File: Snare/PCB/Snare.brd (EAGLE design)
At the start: 100 x 50 mm, 2 parts

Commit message: Finished Schematic
Finished Schematic
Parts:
- added 100K, 47K, R39, R40, R43: 2k, resistor:0207/10
- added C15, C48: 0.33uF, resistor:C050-024X044
- added C2, C21, C22, C3, C30, C34, C35, C36, C37, C39, C40, C43, C44, C45, C49, C50: 0.1uF, resistor:C050-024X044
- added C20, C38: 1nF, resistor:C050-024X044
- added C23, C41: 2.2u, resistor:C050-024X044
- added C24, C28, C31, C32, C33, C42: 10uF, rcl:E2,5-6
- added C26, C27, C29: 1u, resistor:C050-024X044
- added C46, C47: 33nF, resistor:C050-024X044
- added D6: 200mA/100V/1V, SparkFun-DiscreteSemi:DIODE-1N4148
- added IC1, IC10, IC6, IC7, IC8, IC9: LM741P, linear:DIL08
- added Q3, Q4: 2N2222A, SparkFun-DiscreteSemi:TO-92
- added R1, R3, R4, R45, R47, R48, R49, R5, R58, R59, R60, R61, R7, R9: 10k, resistor:0207/10
- added R10, R57, R62, R8: 10k, rcl:RTRIM64W
- added R2, R36, R53: 100k, resistor:0207/10
- added R34: 680k, resistor:0207/10
- added R35, R54, R56, R6: 1k, resistor:0207/10
- added R38: 4.7k, resistor:0207/10
- added R44, R46: 15k, resistor:0207/10
- added R50: 220, resistor:0207/10
- added R51, R67: 47k, resistor:0207/10
- added R52, R65: 470k, resistor:0207/10
- added R55: 1meg, resistor:0207/10
- added R63: 20 OHM, rcl:RTRIM64W
- added R64: 100, resistor:0207/10
- added R66: 51k, resistor:0207/10
- added T1, T5, T6: 2N3904, transistor:TO92
- added U$1: (no value), Capstone:TO-92
- D1: value 1N4148 -> 200mA/100V/1V
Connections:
- net 0V renamed POT5B
- net POT5 renamed POT3A
- net POT6_7 renamed POT3B
- net POT7 renamed POT4A
- net POT8 renamed POT4B
- net POT9 renamed POT5A
- removed net POT1: SV1.6
- removed net POT2: SV1.5
- removed net POT3: SV1.8
- removed net POT4: SV1.7
- new net CC_INPUT: C23.2, IC1.6, R8.2
- new net LOW_FREQ_WN: IC8.6, R3.2, R45.1
- new net N$1: R3.1, R4.2, R5.1
- new net N$17: T1.2, T5.2
- new net N$2: IC1.2, R6.2, R7.1, R9.1
- new net N$20: C30.1, R34.2, T1.3
- new net N$21: C31.-, C33.-, C34.1, R35.2, R36.2, R40.1
- new net N$23: 100K.2, 47K.1, IC6.2
- new net N$27: IC7.2, R43.2
- new net N$28: 47K.2, C35.1
- new net N$3: R6.1, R8.1
- new net N$30: C32.+, R38.2, T5.1
- new net N$32: C38.1, IC7.3, R44.1
- new net N$33: IC8.2, R1.1, R45.2
- new net N$34: C20.1, IC8.3, R46.2
- new net N$36: C15.2, C43.2, D1.C, R53.2
- new net N$37: C23.1, R47.1, R48.2, T6.2
- new net N$38: C41.1, R49.2, T6.3
- new net N$39: C26.1, C42.+, R50.1, T6.1
- new net N$4: IC1.5, R10.1
- new net N$40: D1.A, Q3.3, R52.2
- new net N$41: C43.1, IC9.3, R54.2
- new net N$42: R63.2, R64.2
- new net N$43: C46.2, IC9.2, R55.2
- new net N$44: C46.1, C47.2
- new net N$45: IC9.1, R57.3
- new net N$46: IC9.5, R57.1
- new net N$48: IC10.3, R59.2, R61.1, R63.1
- new net N$49: IC10.2, R58.1, R60.2, U$1.1
- new net N$5: C31.+, R35.1, T5.3
- new net N$50: IC10.1, R62.3
- new net N$51: C48.2, D6.C, R66.2
- new net N$52: IC10.5, R62.1
- new net N$53: D6.A, Q4.3, R65.2
- new net N$6: C30.2, C33.+, C34.2, R34.1, R38.1, R39.2
- new net N$7: IC1.1, R10.3
- new net POT1A: C47.1, IC9.6, R55.1, R56.2, SV1.6
- new net POT1B: R7.2, SV1.5
- new net POT2A: IC7.6, R43.1, SV1.8
- new net POT2B: R5.2, SV1.7
- new net VCA_INPUT: R4.1, R58.2, R61.2
- new net VCA_OUT: IC10.6, R60.1, R9.2
- new net VCA_TRIGGER: R66.1, R67.2, U$1.2
- new net WHITE_NOISE: C32.-, C35.2, R36.1
- new net WHITE_NOISE_AMP: 100K.1, C38.2, IC6.6, R2.1, R46.1
- net +12V: now also C22.2, C24.+, C27.2, C3.2, C37.2, C40.2, C45.1, C50.2, IC1.7, IC10.7, IC6.7, IC7.7, IC8.7, IC9.7, Q3.1, Q4.1, R39.1, R47.2, R50.2
- net -12V: now also C2.2, C21.2, C28.-, C29.1, C36.2, C39.2, C44.2, C49.2, IC1.4, IC10.4, IC6.4, IC7.4, IC8.4, IC9.4, R10.2, R40.2, R48.1, R49.1, R57.2, R62.2
- net AGND: now also C15.1, C2.1, C20.2, C21.1, C22.1, C24.-, C26.2, C27.1, C28.+, C29.2, C3.1, C36.1, C37.1, C39.1, C40.1, C42.-, C44.1, C45.2, C48.1, C49.1, C50.1, IC1.3, IC6.3, R1.2, R2.2, R44.2, R51.1, R52.1, R53.1, R54.1, R56.1, R59.1, R64.1, R65.1, R67.1, U$1.3
- net OUTPUT: now also C41.2, R51.2
- net TRIGGER: now also Q3.2, Q4.2
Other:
- board text removed: "Drum - Generic Feb 2019 Koltin Kosik-Harvey"

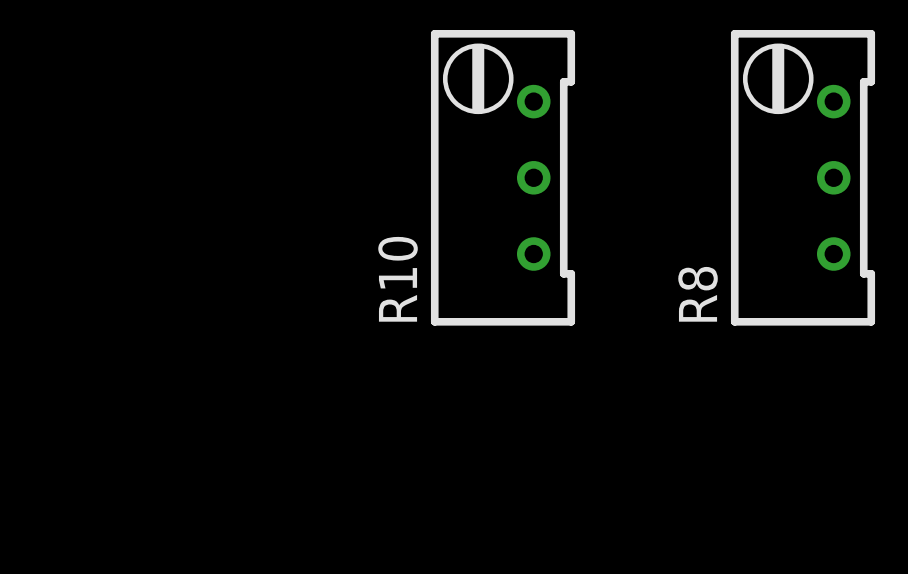
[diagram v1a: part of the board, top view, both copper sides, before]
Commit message: Updated Snare schematic
updated snare schematic
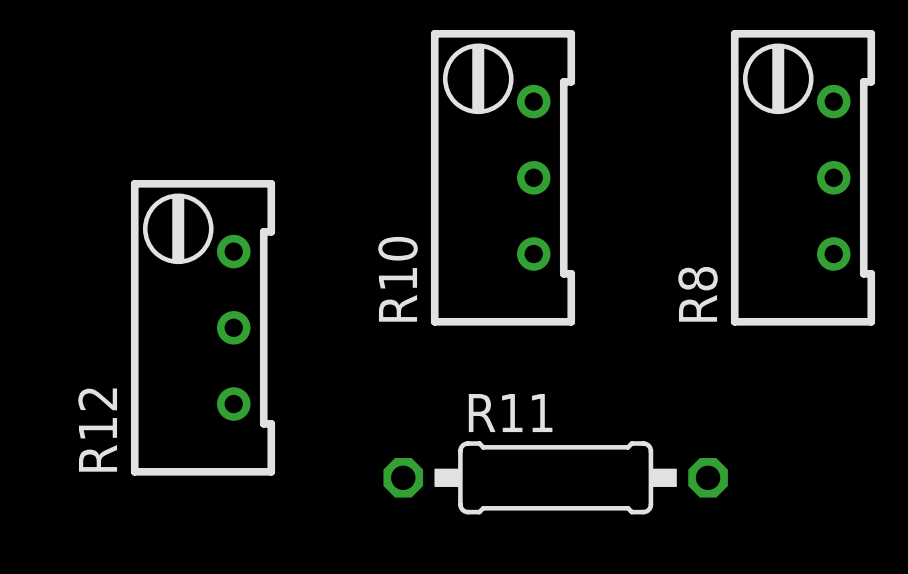
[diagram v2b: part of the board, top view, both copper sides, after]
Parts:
- added R11: 4.7k, resistor:0207/10
- added R12: 10k, rcl:RTRIM64W
- R1: value 10k -> 2k
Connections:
- removed net VCA_OUT: IC10.6, R60.1, R9.2
- new net DRUM_OUTPUT: C47.1, IC9.6, R12.3, R55.1, R56.2
- net AGND: now also R11.2, R12.1
- net N$27: now also R11.1
- net POT1A: now also R12.2; no longer C47.1, IC9.6, R55.1, R56.2
- net SW1: now also IC10.6, R60.1
- net SW2: now also R9.2
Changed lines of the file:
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@@
 <attribute name="VALUE" x="120.7394" y="-148.635" size="1.27" layer="27" ratio="10"/>
 </element>
-<element name="R1" library="resistor" library_urn="urn:adsk.eagle:library:348" package="0207/10" package3d_urn="urn:adsk.eagle:package:25939/1" value="10k" x="4" y="-160" smashed="yes">
+<element name="R1" library="resistor" library_urn="urn:adsk.eagle:library:348" package="0207/10" package3d_urn="urn:adsk.eagle:package:25939/1" value="2k" x="4" y="-160" smashed="yes">
 <attribute name="NAME" x="0.952" y="-158.476" size="1.27" layer="25" ratio="10"/>
 <attribute name="VALUE" x="1.7394" y="-160.635" size="1.27" layer="27" ratio="10"/>
@@
 <attribute name="SPICEPREFIXL" value="POT" x="-17" y="-216" size="1.778" layer="27" display="off"/>
 <attribute name="VALUE" x="-12.65" y="-220.95" size="1.27" layer="27" rot="R90"/>
+</element>
+<element name="R11" library="resistor" library_urn="urn:adsk.eagle:library:348" package="0207/10" package3d_urn="urn:adsk.eagle:package:25939/1" value="4.7k" x="-15" y="-226" smashed="yes">
+<attribute name="NAME" x="-18.048" y="-224.476" size="1.27" layer="25" ratio="10"/>
+<attribute name="VALUE" x="-17.2606" y="-226.635" size="1.27" layer="27" ratio="10"/>
+</element>
+<element name="R12" library="rcl" library_urn="urn:adsk.eagle:library:334" package="RTRIM64W" package3d_urn="urn:adsk.eagle:package:23748/1" value="10k" x="-27" y="-221" smashed="yes">
+<attribute name="NAME" x="-29.62" y="-225.95" size="1.27" layer="25" rot="R90"/>
+<attribute name="SPICEMODEL" value="X" x="-27" y="-221" size="1.778" layer="27" display="off"/>
+<attribute name="SPICEPREFIXL" value="POT" x="-27" y="-221" size="1.778" layer="27" display="off"/>
+<attribute name="VALUE" x="-22.65" y="-225.95" size="1.27" layer="27" rot="R90"/>
 </element>
 </elements>
@@
 <signal name="SW2">
 <contactref element="SV1" pad="20"/>
+<contactref element="R9" pad="2"/>
+<wire x1="40.64" y1="12.7" x2="9.08" y2="-221" width="0" layer="19" extent="1-1"/>
 </signal>
 <signal name="SW1">
 <contactref element="SV1" pad="18"/>
+<contactref element="IC10" pad="6"/>
+<contactref element="R60" pad="1"/>
+<wire x1="43.18" y1="12.7" x2="68.27" y2="42.81" width="0" layer="19" extent="1-1"/>
+<wire x1="4" y1="37.92" x2="43.18" y2="12.7" width="0" layer="19" extent="1-1"/>
 </signal>
 <signal name="TRIGGER">
@@
 <contactref element="IC1" pad="3"/>
 <contactref element="C20" pad="2"/>
-<wire x1="165.46" y1="71" x2="172.46" y2="78" width="0" layer="19" extent="1-1"/>
-<wire x1="175.08" y1="64" x2="165.46" y2="71" width="0" layer="19" extent="1-1"/>
-<wire x1="172.46" y1="50" x2="175.08" y2="64" width="0" layer="19" extent="1-1"/>
-<wire x1="170.54" y1="50" x2="172.46" y2="50" width="0" layer="19" extent="1-1"/>
+<contactref element="R11" pad="2"/>
+<contactref element="R12" pad="1"/>
+<wire x1="-9.92" y1="-226" x2="-25.73" y2="-223.54" width="0" layer="19" extent="1-1"/>
+<wire x1="-0.54" y1="-194" x2="-9.92" y2="-226" width="0" layer="19" extent="1-1"/>
+<wire x1="6.46" y1="-194" x2="-0.54" y2="-194" width="0" layer="19" extent="1-1"/>
+<wire x1="9.08" y1="-165" x2="6.46" y2="-194" width="0" layer="19" extent="1-1"/>
+<wire x1="9.08" y1="-160" x2="9.08" y2="-165" width="0" layer="19" extent="1-1"/>
+<wire x1="117.92" y1="-148" x2="9.08" y2="-160" width="0" layer="19" extent="1-1"/>
+<wire x1="117.92" y1="-133" x2="117.92" y2="-148" width="0" layer="19" extent="1-1"/>
+<wire x1="124.46" y1="-125" x2="117.92" y2="-133" width="0" layer="19" extent="1-1"/>
+<wire x1="117.92" y1="-120" x2="124.46" y2="-125" width="0" layer="19" extent="1-1"/>
+<wire x1="130.27" y1="-104" x2="117.92" y2="-120" width="0" layer="19" extent="1-1"/>
+<wire x1="133.92" y1="-105" x2="130.27" y2="-104" width="0" layer="19" extent="1-1"/>
+<wire x1="140.46" y1="-91" x2="133.92" y2="-105" width="0" layer="19" extent="1-1"/>
+<wire x1="147.46" y1="-91" x2="140.46" y2="-91" width="0" layer="19" extent="1-1"/>
+<wire x1="143.92" y1="-75" x2="140.46" y2="-91" width="0" layer="19" extent="1-1"/>
+<wire x1="143.46" y1="-49" x2="143.92" y2="-75" width="0" layer="19" extent="1-1"/>
+<wire x1="155.54" y1="-49" x2="143.46" y2="-49" width="0" layer="19" extent="1-1"/>
+<wire x1="143.92" y1="-35" x2="143.46" y2="-49" width="0" layer="19" extent="1-1"/>
+<wire x1="143.92" y1="-23" x2="143.92" y2="-35" width="0" layer="19" extent="1-1"/>
+<wire x1="165.46" y1="-12" x2="143.92" y2="-23" width="0" layer="19" extent="1-1"/>
+<wire x1="164.92" y1="-7" x2="165.46" y2="-12" width="0" layer="19" extent="1-1"/>
+<wire x1="176.92" y1="3" x2="164.92" y2="-7" width="0" layer="19" extent="1-1"/>
+<wire x1="170.54" y1="15" x2="176.92" y2="3" width="0" layer="19" extent="1-1"/>
+<wire x1="168.27" y1="22" x2="170.54" y2="15" width="0" layer="19" extent="1-1"/>
+<wire x1="170.54" y1="50" x2="168.27" y2="22" width="0" layer="19" extent="1-1"/>
+<wire x1="172.46" y1="50" x2="170.54" y2="50" width="0" layer="19" extent="1-1"/>
 <wire x1="179.46" y1="50" x2="172.46" y2="50" width="0" layer="19" extent="1-1"/>
+<wire x1="175.08" y1="64" x2="172.46" y2="50" width="0" layer="19" extent="1-1"/>
+<wire x1="165.46" y1="71" x2="175.08" y2="64" width="0" layer="19" extent="1-1"/>
+<wire x1="172.46" y1="78" x2="165.46" y2="71" width="0" layer="19" extent="1-1"/>
 <wire x1="165.46" y1="99" x2="172.46" y2="78" width="0" layer="19" extent="1-1"/>
 <wire x1="165.46" y1="106" x2="165.46" y2="99" width="0" layer="19" extent="1-1"/>
-<wire x1="168.27" y1="22" x2="170.54" y2="50" width="0" layer="19" extent="1-1"/>
-<wire x1="170.54" y1="15" x2="168.27" y2="22" width="0" layer="19" extent="1-1"/>
-<wire x1="176.92" y1="3" x2="170.54" y2="15" width="0" layer="19" extent="1-1"/>
-<wire x1="164.92" y1="-7" x2="176.92" y2="3" width="0" layer="19" extent="1-1"/>
-<wire x1="165.46" y1="-12" x2="164.92" y2="-7" width="0" layer="19" extent="1-1"/>
-<wire x1="143.92" y1="-23" x2="165.46" y2="-12" width="0" layer="19" extent="1-1"/>
-<wire x1="143.92" y1="-35" x2="143.92" y2="-23" width="0" layer="19" extent="1-1"/>
-<wire x1="143.46" y1="-49" x2="143.92" y2="-35" width="0" layer="19" extent="1-1"/>
-<wire x1="155.54" y1="-49" x2="143.46" y2="-49" width="0" layer="19" extent="1-1"/>
-<wire x1="143.92" y1="-75" x2="143.46" y2="-49" width="0" layer="19" extent="1-1"/>
-<wire x1="140.46" y1="-91" x2="143.92" y2="-75" width="0" layer="19" extent="1-1"/>
-<wire x1="147.46" y1="-91" x2="140.46" y2="-91" width="0" layer="19" extent="1-1"/>
-<wire x1="133.92" y1="-105" x2="140.46" y2="-91" width="0" layer="19" extent="1-1"/>
-<wire x1="130.27" y1="-104" x2="133.92" y2="-105" width="0" layer="19" extent="1-1"/>
-<wire x1="117.92" y1="-120" x2="130.27" y2="-104" width="0" layer="19" extent="1-1"/>
-<wire x1="124.46" y1="-125" x2="117.92" y2="-120" width="0" layer="19" extent="1-1"/>
-<wire x1="117.92" y1="-133" x2="124.46" y2="-125" width="0" layer="19" extent="1-1"/>
-<wire x1="117.92" y1="-148" x2="117.92" y2="-133" width="0" layer="19" extent="1-1"/>
 <wire x1="83.27" y1="35.19" x2="143.92" y2="-23" width="0" layer="19" extent="1-1"/>
 <wire x1="52.27" y1="36.19" x2="83.27" y2="35.19" width="0" layer="19" extent="1-1"/>
@@
 <wire x1="165.73" y1="216" x2="170.54" y2="209" width="0" layer="19" extent="1-1"/>
 <wire x1="165.46" y1="223" x2="165.73" y2="216" width="0" layer="19" extent="1-1"/>
-<wire x1="9.08" y1="-160" x2="117.92" y2="-148" width="0" layer="19" extent="1-1"/>
-<wire x1="9.08" y1="-165" x2="9.08" y2="-160" width="0" layer="19" extent="1-1"/>
-<wire x1="6.46" y1="-194" x2="9.08" y2="-165" width="0" layer="19" extent="1-1"/>
-<wire x1="-0.54" y1="-194" x2="6.46" y2="-194" width="0" layer="19" extent="1-1"/>
 </signal>
 <signal name="N$5">
@@
 <contactref element="IC7" pad="2"/>
 <contactref element="R43" pad="2"/>
-<wire x1="183.08" y1="71" x2="37.73" y2="35.19" width="0" layer="19" extent="1-1"/>
+<contactref element="R11" pad="1"/>
+<wire x1="37.73" y1="35.19" x2="183.08" y2="71" width="0" layer="19" extent="1-1"/>
+<wire x1="-20.08" y1="-226" x2="37.73" y2="35.19" width="0" layer="19" extent="1-1"/>
 </signal>
 <signal name="N$32">
@@
 <wire x1="129" y1="-102.095" x2="117.92" y2="-138" width="0" layer="19" extent="1-1"/>
 </signal>
-<signal name="VCA_OUT">
-<contactref element="IC10" pad="6"/>
-<contactref element="R60" pad="1"/>
-<contactref element="R9" pad="2"/>
-<wire x1="4" y1="37.92" x2="9.08" y2="-221" width="0" layer="19" extent="1-1"/>
-<wire x1="68.27" y1="42.81" x2="4" y2="37.92" width="0" layer="19" extent="1-1"/>
-</signal>
 <signal name="N$45">
 <contactref element="IC9" pad="1"/>
@@
 <signal name="POT1A">
 <contactref element="SV1" pad="6"/>
-<contactref element="R55" pad="1"/>
-<contactref element="IC9" pad="6"/>
-<contactref element="C47" pad="1"/>
-<contactref element="R56" pad="2"/>
-<wire x1="143.92" y1="-56" x2="25.27" y2="43.81" width="0" layer="19" extent="1-1"/>
-<wire x1="143.46" y1="-68" x2="143.92" y2="-56" width="0" layer="19" extent="1-1"/>
-<wire x1="154.08" y1="-75" x2="143.46" y2="-68" width="0" layer="19" extent="1-1"/>
-<wire x1="58.42" y1="12.7" x2="25.27" y2="43.81" width="0" layer="19" extent="1-1"/>
+<contactref element="R12" pad="2"/>
+<wire x1="58.42" y1="12.7" x2="-25.73" y2="-221" width="0" layer="19" extent="1-1"/>
 </signal>
 <signal name="POT1B">
@@
 <wire x1="78.19" y1="35.19" x2="-15.73" y2="-213.46" width="0" layer="19" extent="1-1"/>
 </signal>
+<signal name="DRUM_OUTPUT">
+<contactref element="R55" pad="1"/>
+<contactref element="IC9" pad="6"/>
+<contactref element="C47" pad="1"/>
+<contactref element="R56" pad="2"/>
+<contactref element="R12" pad="3"/>
+<wire x1="143.46" y1="-68" x2="-25.73" y2="-218.46" width="0" layer="19" extent="1-1"/>
+<wire x1="143.92" y1="-56" x2="143.46" y2="-68" width="0" layer="19" extent="1-1"/>
+<wire x1="154.08" y1="-75" x2="143.46" y2="-68" width="0" layer="19" extent="1-1"/>
+<wire x1="25.27" y1="43.81" x2="143.92" y2="-56" width="0" layer="19" extent="1-1"/>
+</signal>
 </signals>

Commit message: Started PCB
Started working on the PCB
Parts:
- removed 100K, 47K: 2k, resistor:0207/10
- added R100: 47k, resistor:0207/10
- added R101: 100k, resistor:0207/10
- moved R11 285.0 mm to (79.0, 43.0), turned to 90 degrees
- moved R12 235.7 mm to (29.0, 8.00)
- moved C27 230.9 mm to (72.0, 13.0), turned to 270 degrees
- moved C30 230.5 mm to (7.00, 37.0), turned to 180 degrees
- moved T1 226.3 mm to (7.00, 31.0), turned to 270 degrees
- moved R5 222.0 mm to (73.0, 31.0), turned to 90 degrees
- moved C29 220.0 mm to (68.0, 13.0), turned to 270 degrees
- moved R4 219.2 mm to (79.0, 31.0), turned to 270 degrees
- moved C28 218.7 mm to (70.0, 20.0), turned to 180 degrees
- moved R34 218.5 mm to (13.0, 43.0), turned to 270 degrees
- moved T5 218.5 mm to (13.0, 31.0), turned to 270 degrees
- moved R3 213.5 mm to (76.0, 31.0), turned to 90 degrees
- moved R1 210.1 mm to (50.0, 45.0)
- moved C31 209.3 mm to (20.0, 31.0), turned to 270 degrees
- moved R2 204.8 mm to (48.0, 35.0), turned to 270 degrees
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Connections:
- net N$23: now also R100.1, R101.2; no longer 100K.2, 47K.1
- net N$28: now also R100.2; no longer 47K.2
- net WHITE_NOISE_AMP: now also R101.1; no longer 100K.1
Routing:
- net WHITE_NOISE_AMP: track 0.00 -> 54.2 mm, vias 0 -> 2
- net N$21: track 0.00 -> 54.2 mm
- net LOW_FREQ_WN: track 0.00 -> 41.0 mm
- net N$30: track 0.00 -> 31.6 mm
- net N$6: track 0.00 -> 30.4 mm
- net N$32: track 0.00 -> 21.2 mm, vias 0 -> 2
- net WHITE_NOISE: track 0.00 -> 19.5 mm
- net N$33: track 0.00 -> 18.7 mm
- net N$34: track 0.00 -> 18.6 mm
- net N$23: track 0.00 -> 17.4 mm
- net N$5: track 0.00 -> 15.9 mm
- net N$20: track 0.00 -> 9.62 mm
- net N$17: track 0.00 -> 6.00 mm
- net N$28: track 0.00 -> 3.21 mm
- added copper zone on layer 16, net +12V
- added copper zone on layer 1, net AGND
- removed copper zone on layer 1, net +12V
- removed copper zone on layer 16, net POT5B
